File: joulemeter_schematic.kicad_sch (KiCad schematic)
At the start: 35 parts, among them J1 XT60-M, J2 XT60-M, J3 22035035, U1 LTC1258CMS8-5-PBF, U2 MCP6286T-E/OT, U3 INA240A1PWR, U4 ADS131M04IRUKR

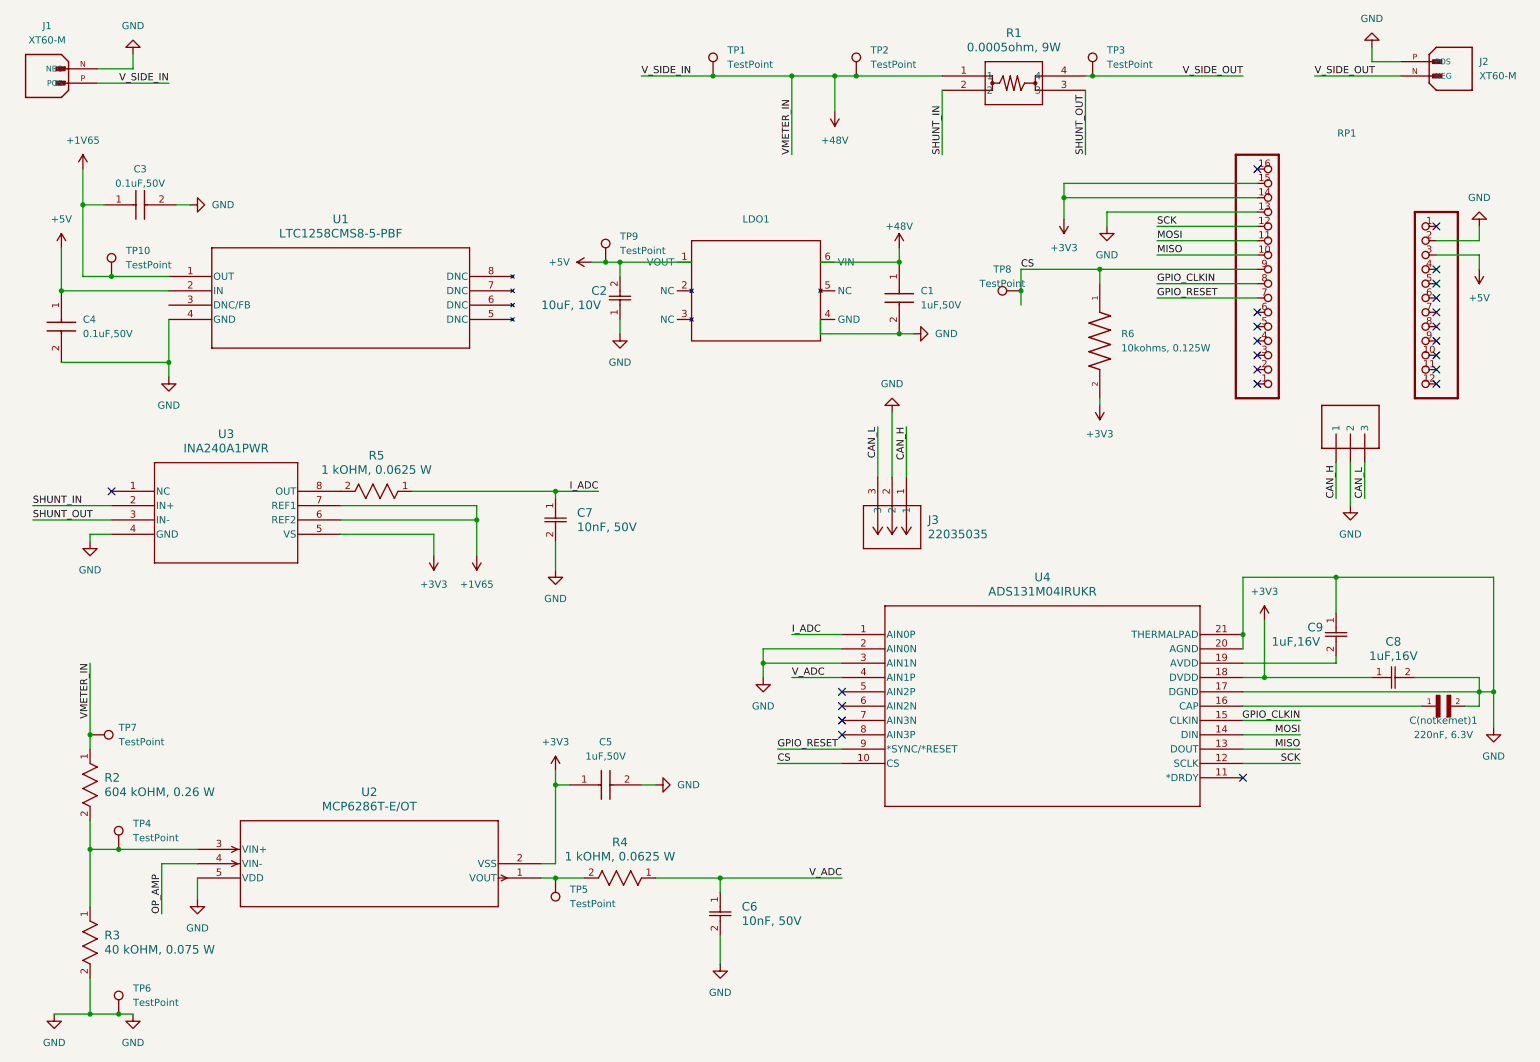
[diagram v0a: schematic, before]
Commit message: edwin's revised schematic 12/24
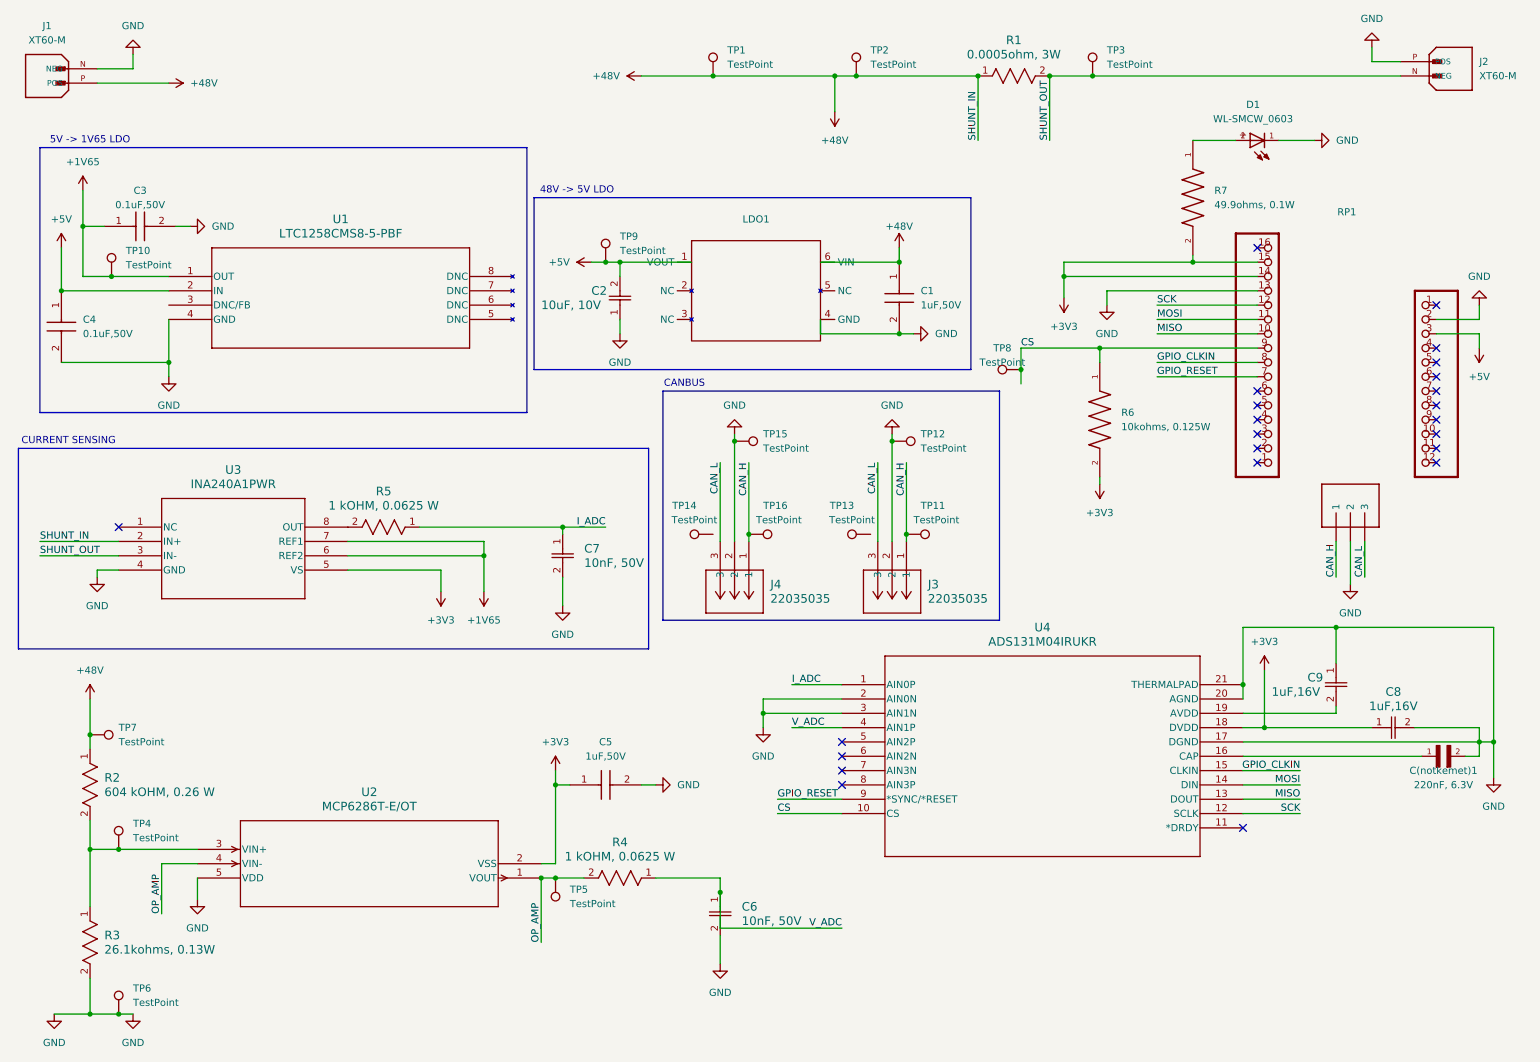
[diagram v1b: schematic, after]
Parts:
- removed R1: 0.0005ohm, 9W, BVB-Z-R0005_ISA, symbol SMV_Custom:BVB-Z-R0005-1.0
- removed R3: 40 kOHM, 0.075 W, RES_TNPW0201_VIS, symbol SMV_Custom:TNPW020140K0DEED
- added D1: WL-SMCW_0603, WL-SMCW_0603:WL-SMCW_0603, symbol SMV_Custom:WL-SMCW_0603
- added J4: 22035035, CON_22035035_MOL, symbol SMV_Custom:3-pin Mini Molex Spox
- added R1: 0.0005ohm, 3W, RES_PU3921_.5mOHM_YAG, symbol SMV_Custom:PU3921FKM130U5L
- added R3: 26.1kohms, 0.13W, RES_TNPW0402_VIS, symbol SMV_Custom:TNPW040226K1BEED
- added R7: 49.9ohms, 0.1W, CRCW060349R9FKEAC:RESC1608X55N, symbol SMV_Custom:CRCW060349R9FKEAC
- added TP11, TP12, TP13, TP14, TP15, TP16: TestPoint, TestPoint:TestPoint_Pad_3.0x3.0mm, symbol Connector:TestPoint
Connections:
- net SHUNT_IN is gone; now on net +48V: U3.2 (IN+)
- net V_SIDE_OUT is gone; now on net SHUNT_OUT: J2.N (NEG), TP3.1
- net +3V3: now also R7.2
- net +48V: now also R1.1
- net CAN_H: now also J4.1, TP11.1, TP16.1
- net CAN_L: now also J4.3
- net GND: now also D1.1, J4.2, R3.2, TP12.1, TP15.1
- net OP_AMP: now also R4.2, TP5.1, U2.1 (VOUT)
- net SHUNT_OUT: now also R1.2
- net at R2.2, TP4.1, U2.3 (VIN+): now also R3.1
- new net: D1.2, R7.1
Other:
- note added: "48V -> 5V LDO"
- note added: "5V -> 1V65 LDO"
- note added: "CANBUS"
- note added: "CURRENT SENSING"
- moved on the sheet: C(notkemet)1, C3, C7, C8, C9, J3, R5, R6, RP1, TP8, U3, U4
